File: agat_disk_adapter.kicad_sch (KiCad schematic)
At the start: 18 parts, among them J1 КОНТРОЛЛЕР, J10 PIN_32, J2_A1 ИЗОТ, J2_B2 ИЗОТ, J3 IDC‐20, J4 GOTEK, J5 Питание GOTEK, J6 ВБ, J7 Джамперы, J8 ВБ2, J9 PIN_32, J9_A1 КОНТРОЛЛЕР, J9_B2 КОНТРОЛЛЕР

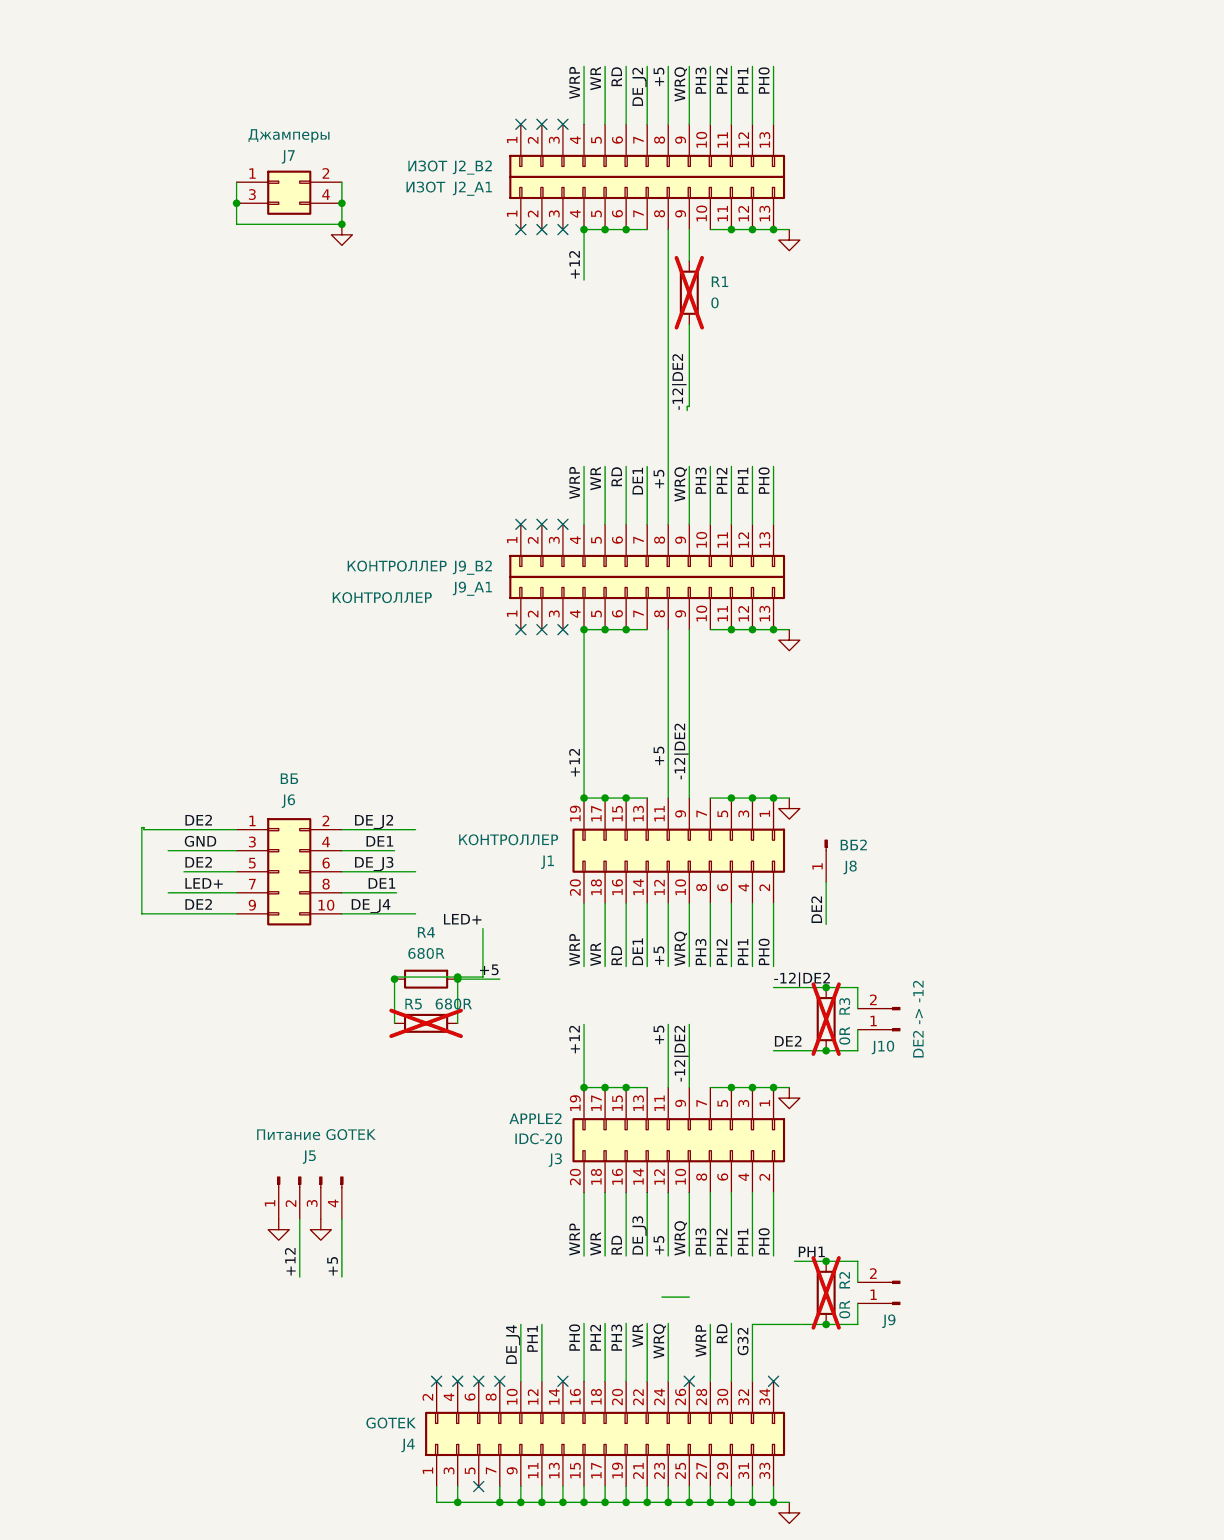
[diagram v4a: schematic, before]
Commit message: create symbols and footprints for Eltras; remove unneeded solder-drops; add Agat logos
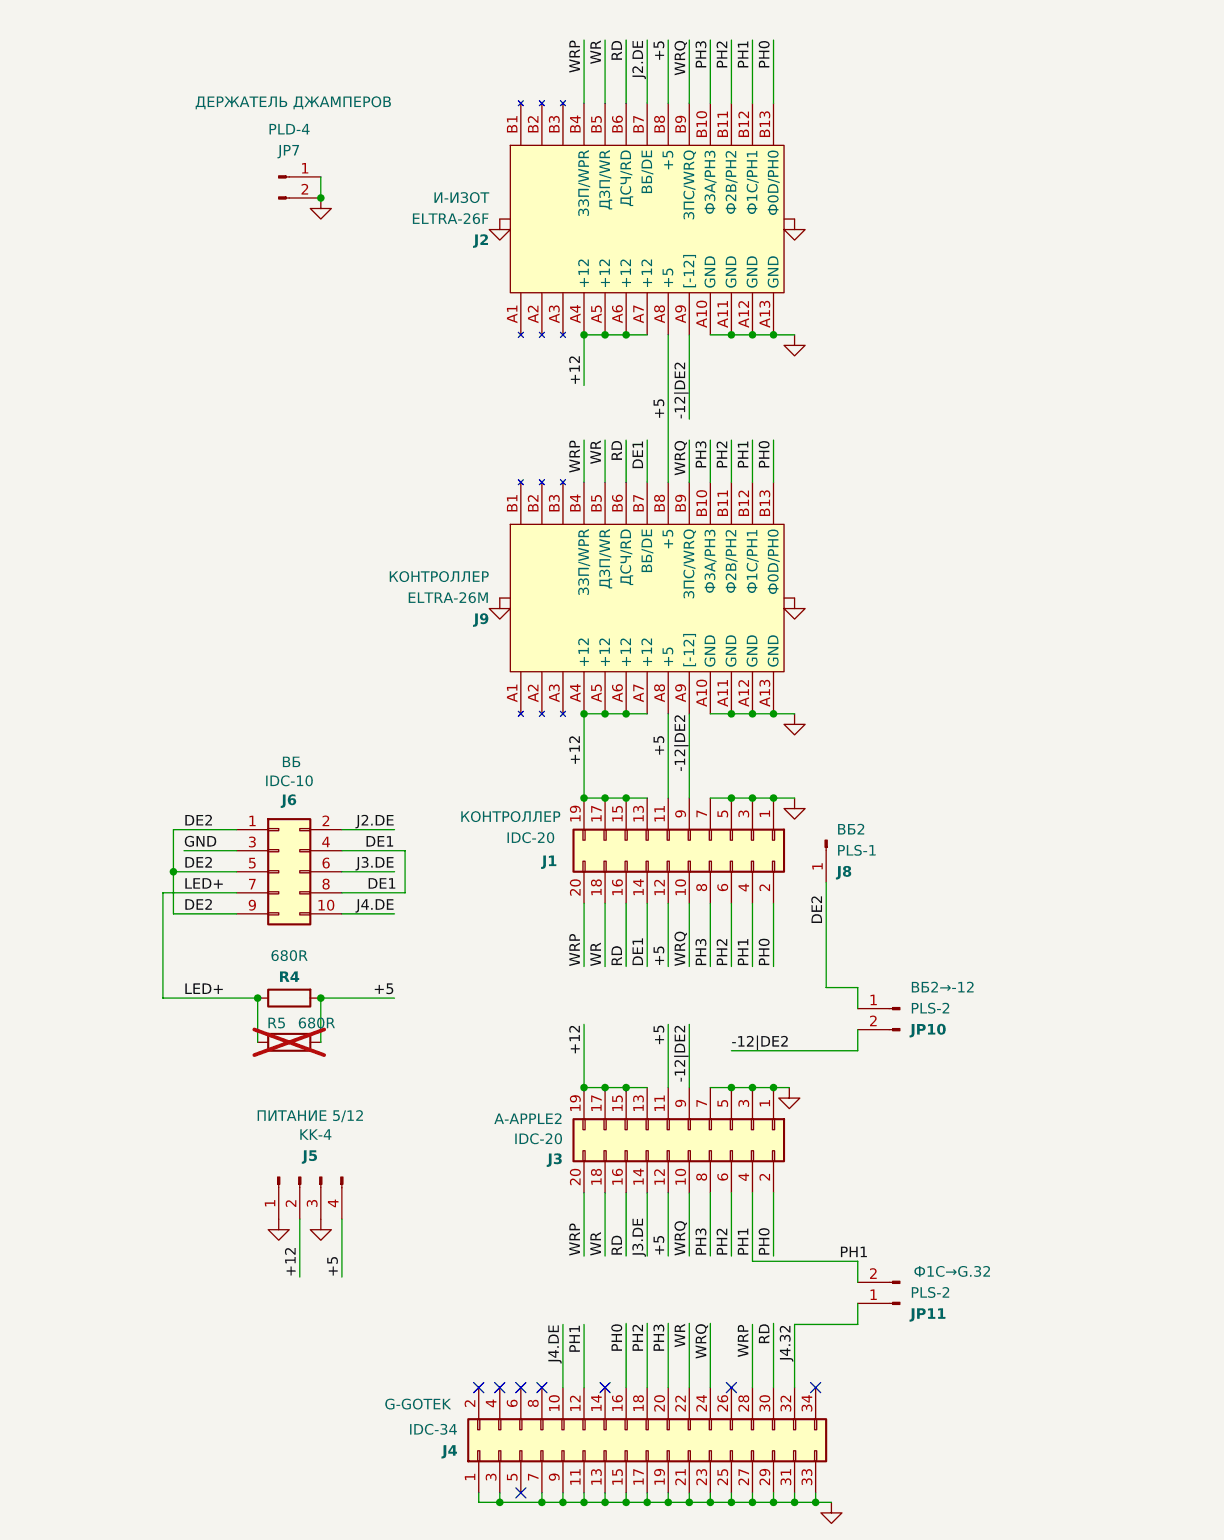
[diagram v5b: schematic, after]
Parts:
- removed J2_A1, J2_B2: ИЗОТ, Connector_JST:JST_EH_B13B-EH-A_1x13_P2.50mm_Vertical, symbol Connector_Generic:Conn_01x13
- removed J9_A1, J9_B2: КОНТРОЛЛЕР, Connector_JST:JST_EH_B13B-EH-A_1x13_P2.50mm_Vertical, symbol Connector_Generic:Conn_01x13
- removed R1: 0, agat_disk_adapter:0R_1206_solder_drop_jumper, symbol Device:R
- removed R2: 0R, agat_disk_adapter:0R_1206_solder_drop_jumper, symbol Device:R
- removed R3: 0R, Resistor_SMD:R_1206_3216Metric, symbol Device:R
- added J2: ELTRA‐26F, symbol agat_disk_adapter:Eltra-26F
- added J9: ELTRA‐26M, symbol agat_disk_adapter:Eltra-26M
- J1: value КОНТРОЛЛЕР -> IDC‐20; footprint Connector_IDC:IDC-Header_2x10_P2.54mm_Vertical -> agat_disk_adapter:IDC-20_header_vertical_rotation180; Function (none) -> КОНТРОЛЛЕР
- J3: footprint Connector_IDC:IDC-Header_2x10_P2.54mm_Vertical -> agat_disk_adapter:IDC-20_header_vertical_rotation180; Function APPLE2 -> A-APPLE2
- J4: value GOTEK -> IDC‐34; footprint Connector_IDC:IDC-Header_2x17_P2.54mm_Vertical -> agat_disk_adapter:IDC-34_header_vertical_rotation0; Function (none) -> G-GOTEK
- J5: value Питание GOTEK -> KK‐4; footprint Connector_Molex:Molex_KK-254_AE-6410-04A_1x04_P2.54mm_Vertical -> agat_disk_adapter:Molex_KK-4_vertical_rotation0; Function (none) -> ПИТАНИЕ 5/12
- J6: value ВБ -> IDC‐10; footprint Connector_IDC:IDC-Header_2x05_P2.54mm_Vertical -> agat_disk_adapter:IDC-10_header_vertical_rotation270; Function (none) -> ВБ
- J8: value ВБ2 -> PLS-1; footprint Connector_PinHeader_2.54mm:PinHeader_1x01_P2.54mm_Horizontal -> Connector_PinHeader_2.00mm:PinHeader_1x01_P2.00mm_Vertical; Function (none) -> ВБ2
- JP10: renamed from J10; value PIN_32 -> PLS-2; footprint Connector_PinHeader_2.54mm:PinHeader_1x02_P2.54mm_Horizontal -> agat_disk_adapter:jumper_pins_solder_drop_vertical; Function (none) -> ВБ2→-12
- JP11: renamed from J9; value PIN_32 -> PLS-2; footprint Connector_PinHeader_2.54mm:PinHeader_1x02_P2.54mm_Horizontal -> agat_disk_adapter:jumper_pins_solder_drop_vertical; Function (none) -> Ф1C→G.32
- JP7: renamed from J7; value Джамперы -> PLD‐4; footprint Connector_PinHeader_2.54mm:PinHeader_2x02_P2.54mm_Vertical -> Connector_PinHeader_2.54mm:PinHeader_1x02_P2.54mm_Vertical; symbol Connector_Generic:Conn_02x02_Odd_Even -> Connector:Conn_01x02_Pin; Function (none) -> ДЕРЖАТЕЛЬ ДЖАМПЕРОВ
- R5: footprint agat_disk_adapter:0R_1206_solder_drop_jumper -> agat_disk_adapter:jumper_1206_solder_drop
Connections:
- net +12: now also J2.A4 (+12), J2.A5 (+12), J2.A6 (+12), J2.A7 (+12), J9.A4 (+12), J9.A5 (+12), J9.A6 (+12), J9.A7 (+12)
- net +5: now also J2.A8 (+5), J2.B8 (+5), J9.A8 (+5), J9.B8 (+5); no longer J6.7 (Pin_7), R4.1, R5.2
- net -12|DE2: now also J2.A9 ([-12]), J9.A9 ([-12])
- net DE1: now also J9.B7 (ВБ/DE)
- net GND: now also J2.A10 (GND), J2.A11 (GND), J2.A12 (GND), J2.A13 (GND), J2.SCREW_L, J2.SCREW_R, J9.A10 (GND), J9.A11 (GND), J9.A12 (GND), J9.A13 (GND), J9.SCREW_L, J9.SCREW_R; no longer JP7.3 (Pin_3), JP7.4 (Pin_4)
- net PH0: now also J2.B13 (Ф0D/PH0), J9.B13 (Ф0D/PH0)
- net PH1: now also J2.B12 (Ф1C/PH1), J9.B12 (Ф1C/PH1)
- net PH2: now also J2.B11 (Ф2B/PH2), J9.B11 (Ф2B/PH2)
- net PH3: now also J2.B10 (Ф3A/PH3), J9.B10 (Ф3A/PH3)
- net RD: now also J2.B6 (ДСЧ/RD), J9.B6 (ДСЧ/RD)
- net WR: now also J2.B5 (ДЗП/WR), J9.B5 (ДЗП/WR)
- net WRP: now also J2.B4 (ЗЗП/WPR), J9.B4 (ЗЗП/WPR)
- net WRQ: now also J2.B9 (ЗПС/WRQ), J9.B9 (ЗПС/WRQ)
- net DE_J2 renamed J2.DE
- net J2.DE: now also J2.B7 (ВБ/DE)
- net DE_J3 renamed J3.DE
- net DE_J4 renamed J4.DE
- net G32 renamed J4.32
- new net LED+: J6.7 (Pin_7), R4.1, R5.2
- no-connect marks 20 -> 8
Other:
- moved on the sheet: J4, JP10, R4, R5

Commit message: improve silkscreen, fix DRC issues, fix jumper holder pins connection to GND; improve schematics
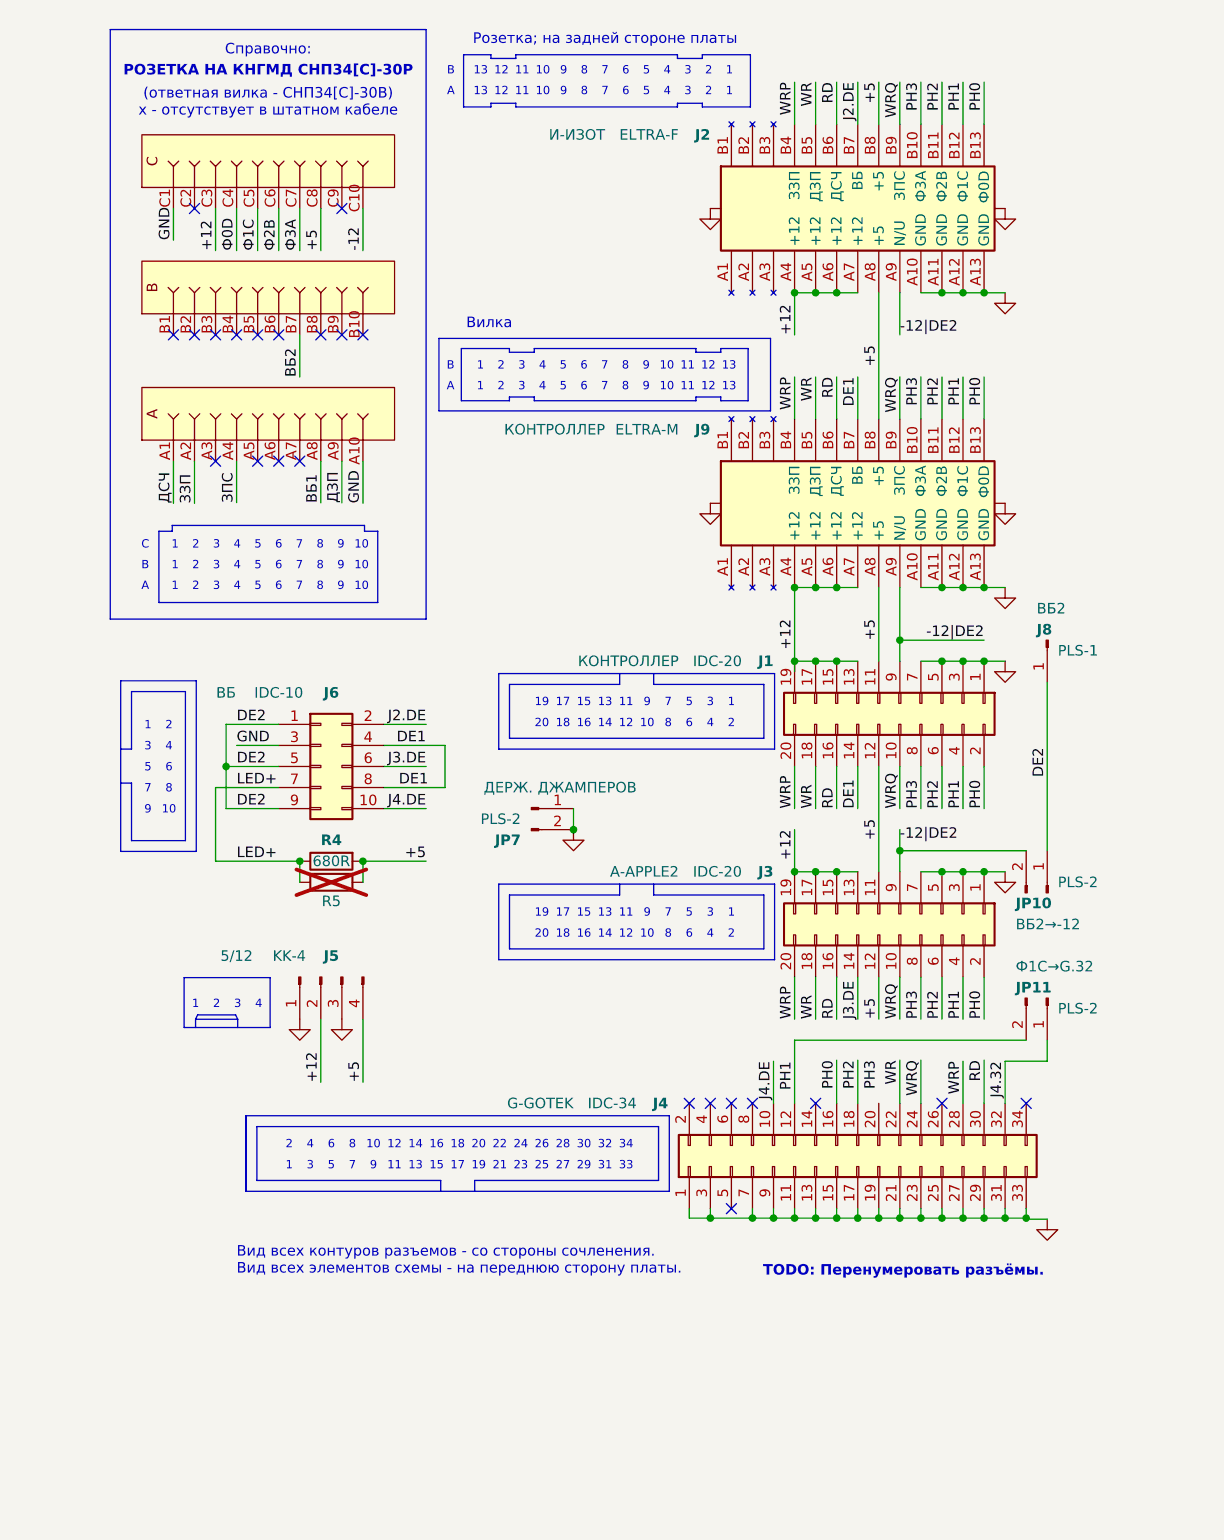
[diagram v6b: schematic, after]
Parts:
- added ~: СНП34С-30/44-12, agat-lib:СНП34С-30, symbol agat-lib:СНП34С-30/44-12
- J2: value ELTRA‐26F -> ELTRA‐F
- J5: Function ПИТАНИЕ 5/12 -> 5/12
- J9: value ELTRA‐26M -> ELTRA‐M
- JP7: value PLD‐4 -> PLS‐2; Function ДЕРЖАТЕЛЬ ДЖАМПЕРОВ -> ДЕРЖ. ДЖАМПЕРОВ
- R5: value 680R -> 0R
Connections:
- net +12: now also ~.C3
- net +5: now also ~.C8
- net GND: now also ~.A10, ~.C1
- net PH3: no longer J4.20 (Pin_20)
- new net -12: ~.C10
- new net ВБ1: ~.A8
- new net ВБ2: ~.B7
- new net ДЗП: ~.A9
- new net ДСЧ: ~.A1
- new net ЗЗП: ~.A2
- new net ЗПС: ~.A4
- new net Ф0D: ~.C4
- new net Ф1C: ~.C5
- new net Ф2B: ~.C6
- new net Ф3A: ~.C7
- no-connect marks 8 -> 23
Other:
- note added: "(ответная вилка - СНП34[С]-30В) х - отсутствует в штатном кабеле"
- note added: "1"
- note added: "10"
- note added: "11"
- note added: "12"
- note added: "13"
- note added: "14"
- note added: "15"
- note added: "16"
- note added: "17"
- note added: "18"
- note added: "19"
- note added: "2"
- note added: "20"
- note added: "21"
- note added: "22"
- note added: "23"
- note added: "24"
- note added: "25"
- note added: "26"
- note added: "27"
- note added: "28"
- note added: "29"
- note added: "3"
- note added: "30"
- note added: "31"
- note added: "32"
- note added: "33"
- note added: "34"
- note added: "4"
- note added: "5"
- note added: "6"
- note added: "7"
- note added: "8"
- note added: "9"
- note added: "A"
- note added: "B"
- note added: "C"
- note added: "TODO: Перенумеровать разъёмы."
- note added: "Вид всех контуров разъемов - со стороны сочленения. Вид всех элементов схемы - на переднюю сторону платы."
- note added: "Вилка"
- note added: "РОЗЕТКА НА КНГМД СНП34[С]-30Р"
- note added: "Розетка; на задней стороне платы"
- note added: "Справочно:"
- company: (none) -> КИБЕР-МУЗЕЙ, МУРОМ
- title: (none) -> AGAT DISK ADAPTER
- moved on the sheet: J1, J2, J3, J4, J5, J6, J8, J9, JP10, JP11, JP7, R4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

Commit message: refactor: rename refs for connectors and jumpers
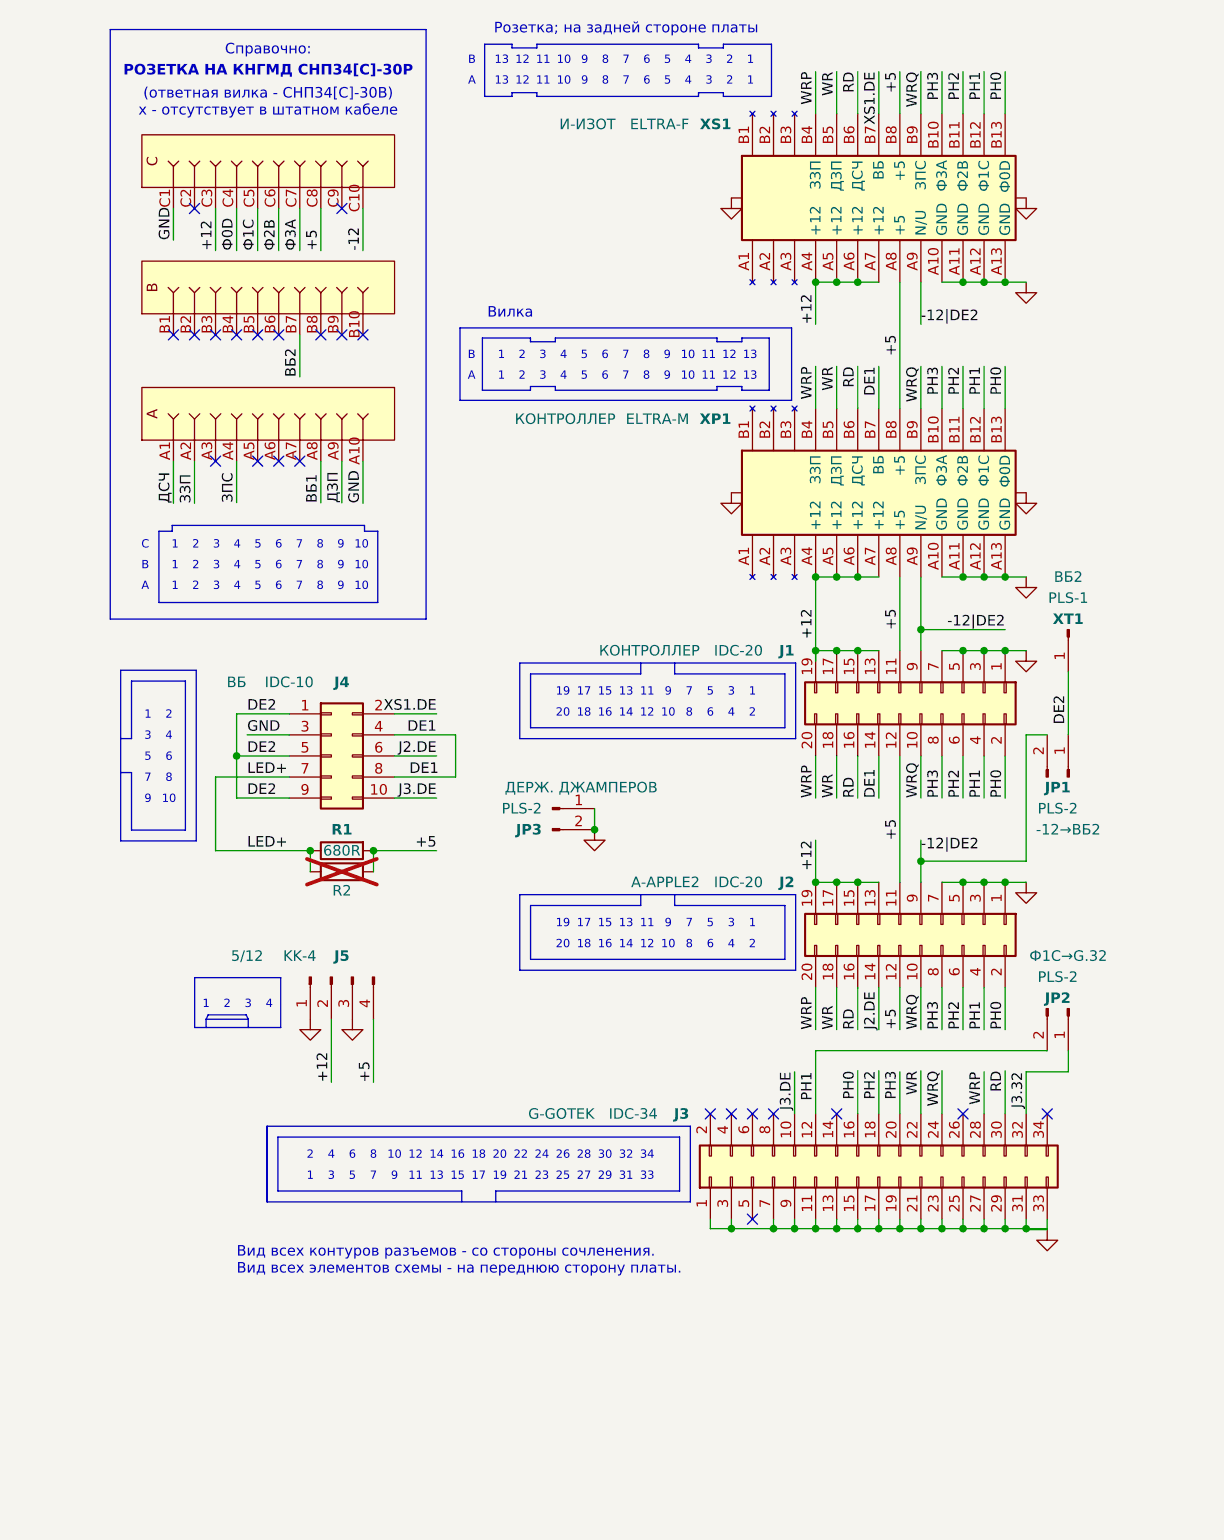
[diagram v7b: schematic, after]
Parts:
- JP1: renamed from JP10; Function ВБ2→-12 -> -12→ВБ2
- renumbered J3 to J2, J4 to J3, J6 to J4, JP11 to JP2, JP7 to JP3, R4 to R1, R5 to R2, J9 to XP1, J2 to XS1, J8 to XT1
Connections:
- net J4.DE is gone; now on net J3.DE: J3.10 (Pin_10), J4.10 (Pin_10)
- net J2.DE: now also J2.14 (Pin_14), J4.6 (Pin_6); no longer J4.2 (Pin_2), XS1.B7 (ВБ)
- net J3.DE: no longer J2.14 (Pin_14), J4.6 (Pin_6)
- net J4.32 renamed J3.32
- new net XS1.DE: J4.2 (Pin_2), XS1.B7 (ВБ)
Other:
- note removed: "TODO: Перенумеровать разъёмы."
- moved on the sheet: J1, J2, J3, J4, J5, JP1, JP2, JP3, R1, R2, XP1, XS1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
